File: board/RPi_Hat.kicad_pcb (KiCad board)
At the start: 2 copper layers, 65 x 56.5 mm, 46 parts, among them IC1 ATMEGA328-A, IC2 RFM69HW, J1 RPi_GPIO, P1 FTDI_CONN_01X06, P10 SW_CONN, P11 BATT_IN, P12 CONN_01X01, P13 ICSP, P2 D8, P3 A0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

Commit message: rev3 board draft
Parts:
- added R11: 4.7K, Resistors_SMD:R_0603_HandSoldering, F.Cu at (99.4, 90.8)
- added R12: 10K, Resistors_SMD:R_0603_HandSoldering, F.Cu at (99.4, 86.2)
- I1: footprint TO_SOT_Packages_SMD:SOT-23_Handsoldering -> TO_SOT_Packages_SMD:SOT-223
- moved C4 8.55 mm to (126.0, 70.8)
- moved R2 6.99 mm to (132.2, 60.6)
- moved P8 5.17 mm to (104.8, 97.0), turned to 90 degrees
- moved P7 5.17 mm to (104.8, 94.5), turned to 90 degrees
- moved P6 5.16 mm to (104.8, 91.8), turned to 90 degrees
- moved P5 5.16 mm to (104.8, 89.2), turned to 90 degrees
- moved P4 5.16 mm to (104.8, 86.7), turned to 90 degrees
- moved P3 5.16 mm to (104.8, 84.0), turned to 90 degrees
- moved P2 5.16 mm to (104.8, 81.5), turned to 90 degrees
- moved R7 4.42 mm to (95.0, 86.5)
- moved R9 4.42 mm to (90.0, 85.5)
- moved SW4 4.42 mm to (90.0, 94.5)
- moved R10 4.42 mm to (92.6, 83.0)
- moved R8 4.42 mm to (87.4, 87.7)
- moved P12 4.00 mm to (80.4, 88.2)
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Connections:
- P2 pad 2: TEMP_D8 -> V3.3
- P2 pad 3: V3.3 -> TEMP_D8
- P3 pad 2: ADC0 -> V3.3
- P3 pad 3: V3.3 -> ADC0
- P4 pad 2: ADC1 -> V3.3
- P4 pad 3: V3.3 -> ADC1
- P5 pad 2: ADC2 -> V3.3
- P5 pad 3: V3.3 -> ADC2
- P6 pad 2: ADC3 -> V3.3
- P6 pad 3: V3.3 -> ADC3
- P7 pad 2: ADC4 -> V3.3
- P7 pad 3: V3.3 -> ADC4
- P8 pad 2: ADC5 -> V3.3
- P8 pad 3: V3.3 -> ADC5
- SW2 pad 1: Net-(C5-Pad1) -> RST
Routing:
- net TEMP_D8: track 28.9 -> 60.9 mm, vias 1 -> 0
- net D10_SS: track 18.2 -> 35.4 mm, vias 1 -> 3
- net RST: track 49.4 -> 64.1 mm
- net LED_D9: track 56.9 -> 68.8 mm
- net GND: track 93.7 -> 83.6 mm, vias 12 -> 9
- net Net-(C5-Pad1): track 71.8 -> 61.8 mm
- net V3.3: track 146.0 -> 156.0 mm, vias 5 -> 4
- net NODE_ID_8: track 36.0 -> 42.9 mm
- net NODE_ID_1: track 41.3 -> 48.0 mm
- net V3.3_BAT: track 42.6 -> 36.2 mm
- net +BATT: track 104.4 -> 99.0 mm
- net NODE_ID_2: track 53.7 -> 58.6 mm
- net NODE_ID_4: track 42.3 -> 47.2 mm
- net Net-(IC2-Pad10): track 12.7 -> 16.7 mm
- net ADC2: track 26.8 -> 24.0 mm, vias 1 -> 0
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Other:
- board text added: "+"
- board text added: "-"
- board text added: "4.7K"
- board text added: "G"
- board text added: "S"
- board text added: "V"
- board text added: "rev.3"
- board text added: "rev.3 2017-01-04"
- board text removed: "+BATT"
- board text removed: "-GND"
- board text removed: "3.3V"
- board text removed: "NC"
- board text removed: "SIG"
- board text removed: "rev.2"
- board text removed: "rev.2 2016-07-06"

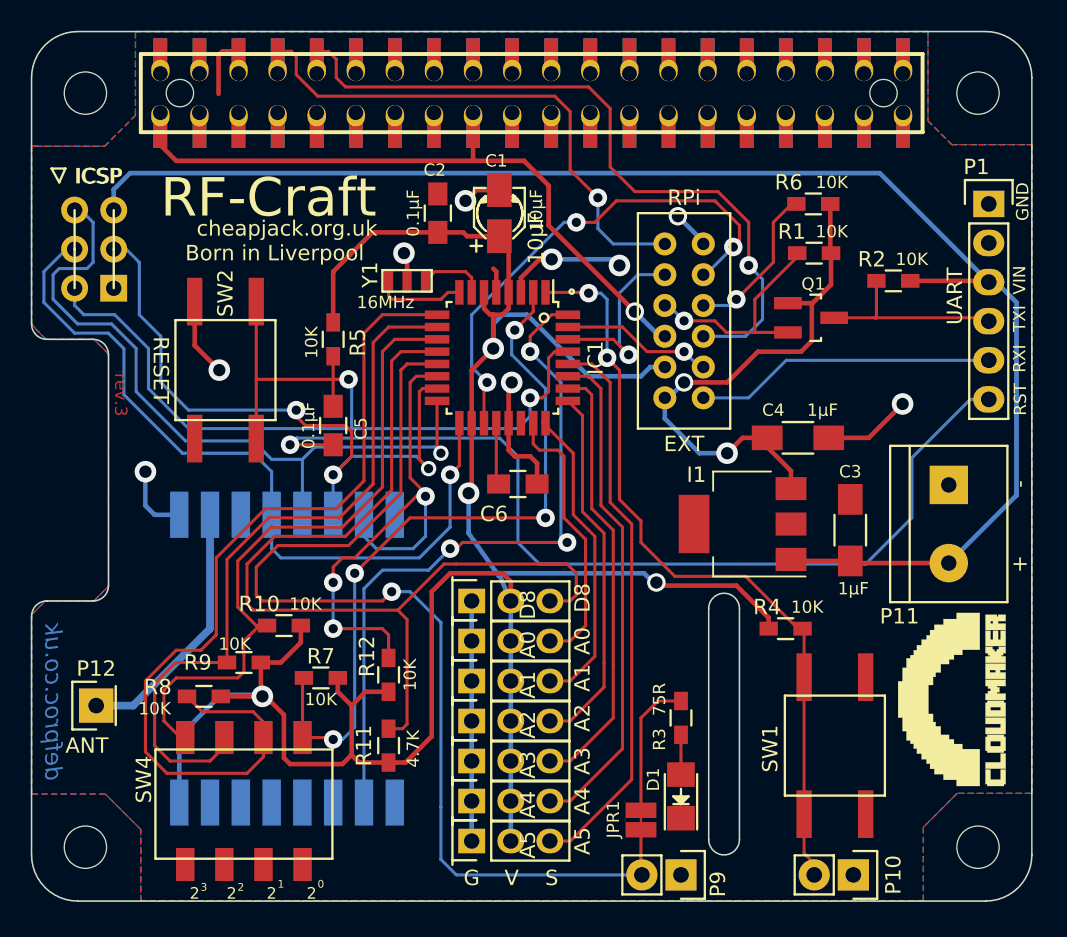
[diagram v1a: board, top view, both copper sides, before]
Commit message: new logo, and rev3 layout
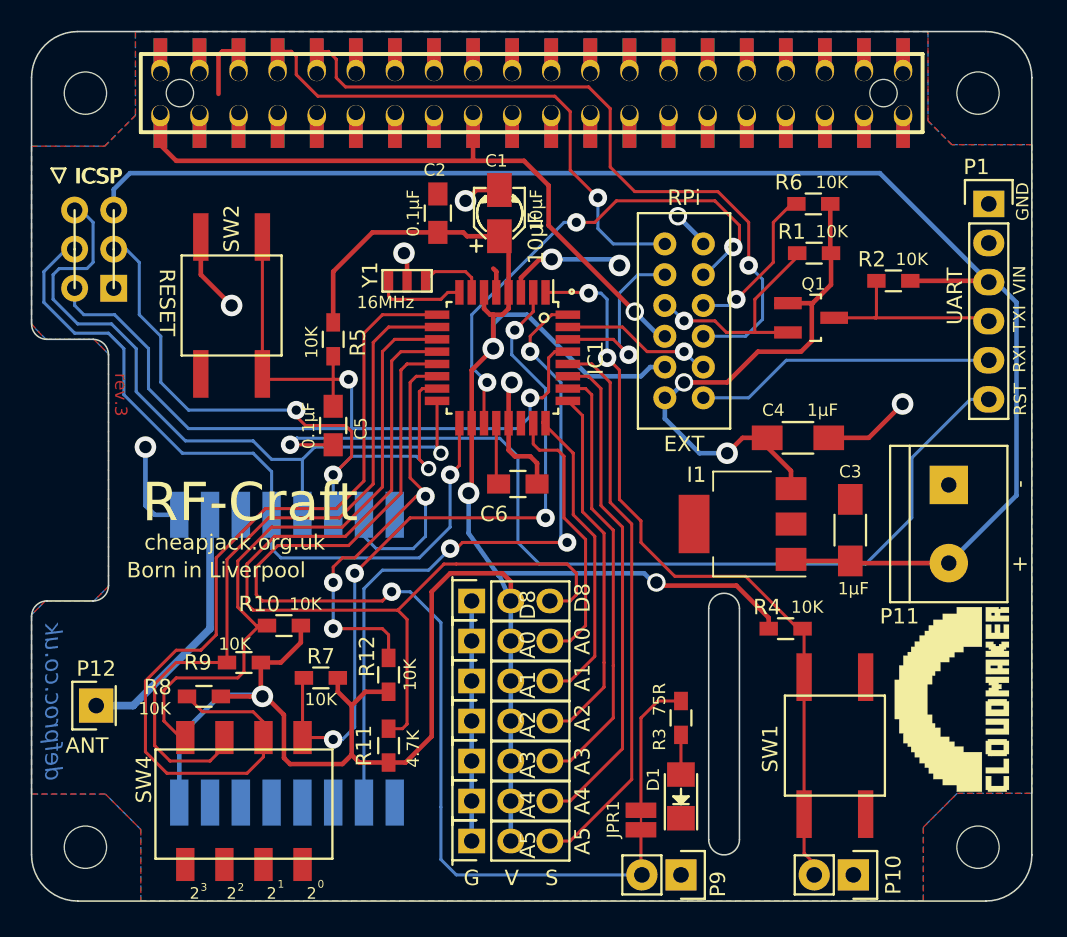
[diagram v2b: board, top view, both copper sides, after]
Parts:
- moved SW2 4.22 mm to (89.2, 62.2)
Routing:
- net GND: track 83.6 -> 85.4 mm
- net RST: track 64.1 -> 63.2 mm
